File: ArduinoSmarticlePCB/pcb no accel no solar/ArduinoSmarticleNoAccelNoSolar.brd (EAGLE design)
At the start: 48.9 x 17.4 mm, 9 parts

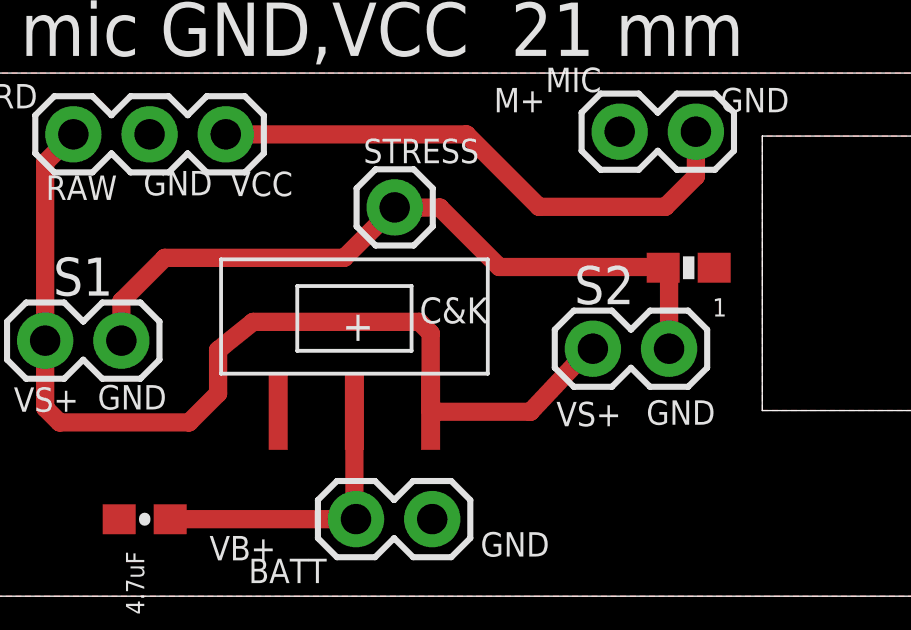
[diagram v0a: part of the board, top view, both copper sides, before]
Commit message: increased isolation size
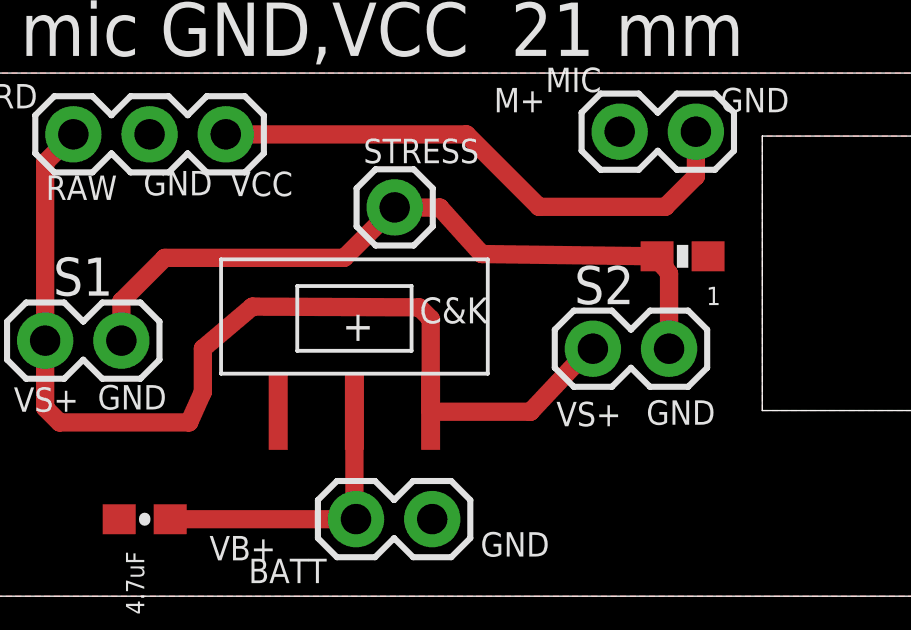
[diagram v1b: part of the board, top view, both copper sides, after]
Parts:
- moved R1 0.43 mm to (35.1, 11.3)
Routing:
- net V_BATT: track 33.8 -> 34.8 mm
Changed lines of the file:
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@@
 <attribute name="NAME" x="16.104821875" y="11.2867625" size="1.27" layer="21" ratio="10" rot="R180"/>
 </element>
-<element name="R1" library="SparkFun-Resistors" package="0603-RES" value="1" x="35.2950625" y="10.9474" smashed="yes" rot="R180">
-<attribute name="PROD_ID" value="RES-08296" x="35.2950625" y="10.9474" size="1.778" layer="27" rot="R180" display="off"/>
-<attribute name="VALUE" value="2.0k" x="35.2950625" y="10.9474" size="1.778" layer="27" rot="R180" display="off"/>
-<attribute name="VALUE" x="36.5650625" y="9.9314" size="0.6096" layer="21" font="vector" rot="R180"/>
+<element name="R1" library="SparkFun-Resistors" package="0603-RES" value="1" x="35.0918625" y="11.3284" smashed="yes" rot="R180">
+<attribute name="PROD_ID" value="RES-08296" x="35.0918625" y="11.3284" size="1.778" layer="27" rot="R180" display="off"/>
+<attribute name="VALUE" value="2.0k" x="35.0918625" y="11.3284" size="1.778" layer="27" rot="R180" display="off"/>
+<attribute name="VALUE" x="36.3618625" y="10.3124" size="0.6096" layer="21" font="vector" rot="R180"/>
 </element>
 <element name="MIC" library="SparkFun-Connectors" package="1X02" value="" x="35.5352" y="15.48288125" smashed="yes" rot="R180">
@@
 <contactref element="BRD" pad="2"/>
 <contactref element="BATT" pad="2"/>
-<polygon width="0.002540625" layer="1" spacing="0.254" isolate="0.3048" thermals="no">
+<polygon width="0.002540625" layer="1" spacing="0.254" isolate="0.6096" thermals="no">
 <vertex x="0.000003125" y="0"/>
 <vertex x="0.000003125" y="6.184659375"/>
@@
 <wire x1="13.844221875" y1="6.272578125" x2="14.3256" y2="5.7912" width="0.6096" layer="1"/>
 <wire x1="14.3256" y1="5.7912" x2="18.6436" y2="5.7912" width="0.6096" layer="1"/>
-<wire x1="18.6436" y1="5.7912" x2="19.6088" y2="6.7564" width="0.6096" layer="1"/>
-<wire x1="19.6088" y1="6.7564" x2="19.6088" y2="8.2042" width="0.6096" layer="1"/>
-<wire x1="19.6088" y1="8.2042" x2="20.7772" y2="9.144" width="0.6096" layer="1"/>
-<wire x1="20.7772" y1="9.144" x2="26.3144" y2="9.144" width="0.6096" layer="1"/>
-<wire x1="26.3144" y1="9.144" x2="26.6954" y2="8.763" width="0.6096" layer="1"/>
-<wire x1="26.6954" y1="8.763" x2="26.6954" y2="6.1493375" width="0.6096" layer="1"/>
+<wire x1="18.6436" y1="5.7912" x2="19.1008" y2="6.8072" width="0.6096" layer="1"/>
+<wire x1="19.1008" y1="6.8072" x2="19.1008" y2="8.255" width="0.6096" layer="1"/>
+<wire x1="19.1008" y1="8.255" x2="20.7518" y2="9.652" width="0.6096" layer="1"/>
+<wire x1="20.7518" y1="9.652" x2="26.3144" y2="9.6266" width="0.6096" layer="1"/>
+<wire x1="26.3144" y1="9.6266" x2="26.6954" y2="9.2456" width="0.6096" layer="1"/>
+<wire x1="26.6954" y1="9.2456" x2="26.6954" y2="6.1493375" width="0.6096" layer="1"/>
 <wire x1="26.6954" y1="6.1493375" x2="26.6928625" y2="6.1468" width="0.6096" layer="1"/>
 <wire x1="26.6928625" y1="6.1468" x2="30.0228" y2="6.1468" width="0.6096" layer="1"/>
@@
 <wire x1="17.8308" y1="11.2776" x2="16.384221875" y2="9.831021875" width="0.6096" layer="1"/>
 <wire x1="16.384221875" y1="9.831021875" x2="16.384221875" y2="8.5181625" width="0.6096" layer="1"/>
-<wire x1="34.6413625" y1="10.7511" x2="34.4450625" y2="10.9474" width="0.6096" layer="1"/>
-<wire x1="34.4450625" y1="10.9474" x2="34.4450625" y2="10.9955375" width="0.6096" layer="1"/>
+<wire x1="34.6413625" y1="10.7511" x2="34.2418625" y2="11.3284" width="0.6096" layer="1"/>
+<wire x1="34.2418625" y1="11.3284" x2="34.4450625" y2="10.9955375" width="0.6096" layer="1"/>
 <wire x1="25.5002625" y1="12.954" x2="25.4948625" y2="12.9594" width="0.6096" layer="1"/>
 <wire x1="34.6413625" y1="10.7511" x2="34.6413625" y2="8.2491375" width="0.6096" layer="1"/>
 <wire x1="25.5002625" y1="12.954" x2="27.0002" y2="12.954" width="0.6096" layer="1"/>
-<wire x1="27.0002" y1="12.954" x2="28.9814" y2="10.9728" width="0.6096" layer="1"/>
-<wire x1="28.9814" y1="10.9728" x2="34.4196625" y2="10.9728" width="0.6096" layer="1"/>
-<wire x1="34.4196625" y1="10.9728" x2="34.4450625" y2="10.9474" width="0.6096" layer="1"/>
+<wire x1="27.0002" y1="12.954" x2="28.3972" y2="11.4046" width="0.6096" layer="1"/>
+<wire x1="28.3972" y1="11.4046" x2="34.2418625" y2="11.3284" width="0.6096" layer="1"/>
 </signal>
 <signal name="SWITCH+">

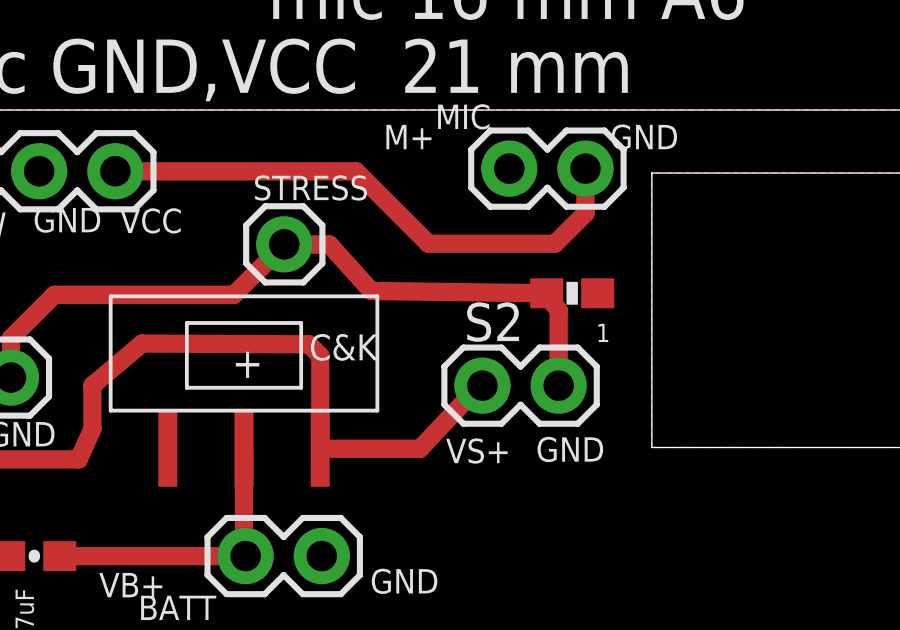
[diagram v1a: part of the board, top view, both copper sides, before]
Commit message: symmetrized path still need to remove concave corners
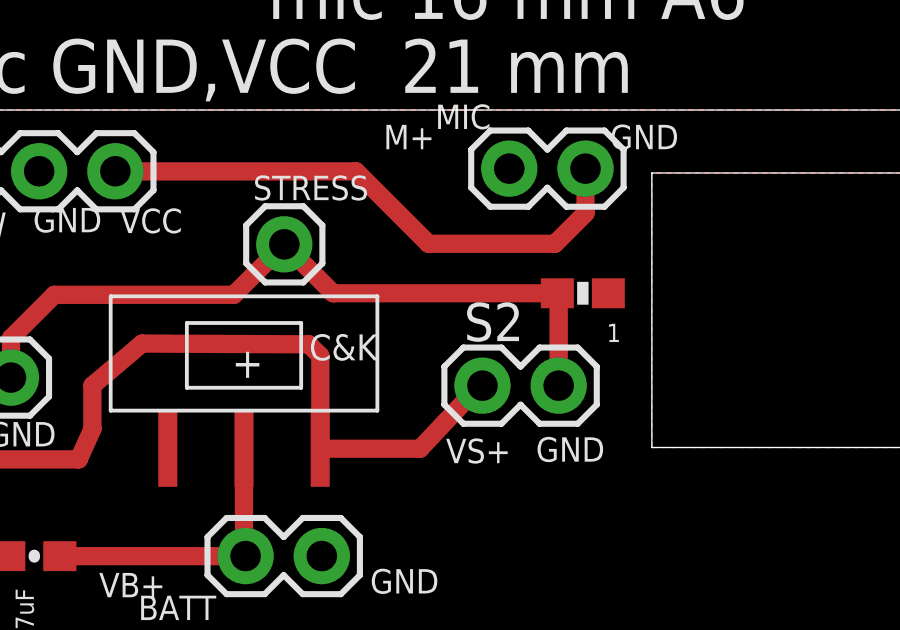
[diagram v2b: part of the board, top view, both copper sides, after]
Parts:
- moved R1 0.36 mm to (35.4, 11.3)
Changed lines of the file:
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@@
 <attribute name="NAME" x="16.104821875" y="11.2867625" size="1.27" layer="21" ratio="10" rot="R180"/>
 </element>
-<element name="R1" library="SparkFun-Resistors" package="0603-RES" value="1" x="35.0918625" y="11.3284" smashed="yes" rot="R180">
-<attribute name="PROD_ID" value="RES-08296" x="35.0918625" y="11.3284" size="1.778" layer="27" rot="R180" display="off"/>
-<attribute name="VALUE" value="2.0k" x="35.0918625" y="11.3284" size="1.778" layer="27" rot="R180" display="off"/>
-<attribute name="VALUE" x="36.3618625" y="10.3124" size="0.6096" layer="21" font="vector" rot="R180"/>
+<element name="R1" library="SparkFun-Resistors" package="0603-RES" value="1" x="35.4474625" y="11.3284" smashed="yes" rot="R180">
+<attribute name="PROD_ID" value="RES-08296" x="35.4474625" y="11.3284" size="1.778" layer="27" rot="R180" display="off"/>
+<attribute name="VALUE" value="2.0k" x="35.4474625" y="11.3284" size="1.778" layer="27" rot="R180" display="off"/>
+<attribute name="VALUE" x="36.7174625" y="10.3124" size="0.6096" layer="21" font="vector" rot="R180"/>
 </element>
 <element name="MIC" library="SparkFun-Connectors" package="1X02" value="" x="35.5352" y="15.48288125" smashed="yes" rot="R180">
@@
 <contactref element="S2" pad="1"/>
 <contactref element="S1" pad="1"/>
-<wire x1="34.6684625" y1="8.2762375" x2="34.6413625" y2="8.2491375" width="0.4064" layer="1"/>
 <wire x1="25.4948625" y1="12.9594" x2="23.8130625" y2="11.2776" width="0.6096" layer="1"/>
 <wire x1="23.8130625" y1="11.2776" x2="17.8308" y2="11.2776" width="0.6096" layer="1"/>
 <wire x1="17.8308" y1="11.2776" x2="16.384221875" y2="9.831021875" width="0.6096" layer="1"/>
 <wire x1="16.384221875" y1="9.831021875" x2="16.384221875" y2="8.5181625" width="0.6096" layer="1"/>
-<wire x1="34.6413625" y1="10.7511" x2="34.2418625" y2="11.3284" width="0.6096" layer="1"/>
-<wire x1="34.2418625" y1="11.3284" x2="34.4450625" y2="10.9955375" width="0.6096" layer="1"/>
-<wire x1="25.5002625" y1="12.954" x2="25.4948625" y2="12.9594" width="0.6096" layer="1"/>
-<wire x1="34.6413625" y1="10.7511" x2="34.6413625" y2="8.2491375" width="0.6096" layer="1"/>
-<wire x1="25.5002625" y1="12.954" x2="27.0002" y2="12.954" width="0.6096" layer="1"/>
-<wire x1="27.0002" y1="12.954" x2="28.3972" y2="11.4046" width="0.6096" layer="1"/>
-<wire x1="28.3972" y1="11.4046" x2="34.2418625" y2="11.3284" width="0.6096" layer="1"/>
+<wire x1="34.5974625" y1="11.3284" x2="27.1258625" y2="11.3284" width="0.6096" layer="1"/>
+<wire x1="27.1258625" y1="11.3284" x2="25.4948625" y2="12.9594" width="0.6096" layer="1"/>
+<wire x1="34.6413625" y1="8.2491375" x2="34.6413625" y2="11.2845" width="0.6096" layer="1"/>
+<wire x1="34.6413625" y1="11.2845" x2="34.5974625" y2="11.3284" width="0.6096" layer="1"/>
 </signal>
 <signal name="SWITCH+">

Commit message: Merediths changes to the PCB, now can be milled on the othermill successfully downstairs
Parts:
- moved S2 4.32 mm to (34.6, 3.93)
- moved R1 2.11 mm to (35.5, 9.22)
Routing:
- net SERVOGND: track 24.6 -> 29.5 mm
- net V_BATT: track 34.8 -> 36.3 mm
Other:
- board text added: "Battery 45mm"
- board text added: "Mic 16mm A6"
- board text added: "Mic GND,VCC 26mm, 26 mm"
- board text added: "RAW, GND, VCC 26mm"
- board text added: "S1 SIG, 48 mm D5"
- board text added: "S1 VCC,GND, 37,38mm"
- board text added: "S2 SIG, 52mm D6"
- board text added: "S2 VCC,GND, 37,38mm"
- board text added: "Stress 28 A7"
- board text removed: "RAW,GND,VCC 26 mm"
- board text removed: "S1 SIG,48 mm D5"
- board text removed: "S1 SIG,52 mm D6"
- board text removed: "S1 VCC,GND 37,38 mm"
- board text removed: "S2 VCC,GND 37,38 mm"
- board text removed: "battery 45 mm"
- board text removed: "mic 16 mm A6"
- board text removed: "mic GND,VCC 21 mm"
- board text removed: "stress 28 mm A7"
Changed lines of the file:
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@@
 <setting verticaltext="up"/>
 </settings>
-<grid distance="0.001" unitdist="inch" unit="inch" style="lines" multiple="1" display="yes" altdistance="0.0001" altunitdist="inch" altunit="inch"/>
+<grid distance="50" unitdist="mil" unit="mil" style="lines" multiple="1" display="no" altdistance="5" altunitdist="mil" altunit="mil"/>
 <layers>
 <layer number="1" name="Top" color="4" fill="1" visible="yes" active="yes"/>
@@
 <text x="23.7464625" y="8.509" size="1.016" layer="21">+</text>
 <text x="21.5366625" y="2.0066" size="0.8128" layer="21" rot="R180">VB+</text>
-<text x="30.6552625" y="2.1336" size="0.8128" layer="21" rot="R180">GND</text>
-<text x="33.8810625" y="5.715" size="0.8128" layer="21">GND</text>
-<text x="30.8838625" y="5.6642" size="0.8128" layer="21">VS+</text>
+<text x="29.3852625" y="0.8636" size="0.8128" layer="21" rot="R180">GND</text>
+<text x="34.2620625" y="1.524" size="0.8128" layer="21">GND</text>
+<text x="31.0108625" y="1.3462" size="0.8128" layer="21">VS+</text>
 <text x="13.8658625" y="13.208" size="0.8128" layer="21">RAW</text>
 <text x="17.1170625" y="13.3604" size="0.8128" layer="21">GND</text>
@@
 <text x="28.8010625" y="16.129" size="0.8128" layer="21">M+</text>
 <wire x1="11.7474625" y1="6.1872" x2="-0.0025375" y2="6.188121875" width="0" layer="20"/>
-<text x="36.9544625" y="29.21" size="1.778" layer="21" rot="R180">RAW,GND,VCC 26 mm</text>
-<text x="37.0052625" y="26.6446" size="1.778" layer="21" rot="R180">battery 45 mm</text>
-<text x="40.8406625" y="24.4094" size="1.778" layer="21" rot="R180">stress 28 mm A7</text>
-<text x="40.9422625" y="22.2504" size="1.778" layer="21" rot="R180">mic 16 mm A6</text>
-<text x="37.5894625" y="-1.4478" size="1.778" layer="21" rot="R180">S1 VCC,GND 37,38 mm</text>
-<text x="41.5518625" y="-6.3754" size="1.778" layer="21" rot="R180">S1 SIG,48 mm D5</text>
-<text x="41.5264625" y="-8.7884" size="1.778" layer="21" rot="R180">S1 SIG,52 mm D6</text>
-<text x="37.6402625" y="-3.9624" size="1.778" layer="21" rot="R180">S2 VCC,GND 37,38 mm</text>
-<text x="37.1322625" y="19.7866" size="1.778" layer="21" rot="R180">mic GND,VCC  21 mm</text>
+<text x="17.78" y="30.48" size="1.778" layer="21">RAW, GND, VCC 26mm</text>
+<text x="17.78" y="27.94" size="1.778" layer="21">Battery 45mm</text>
+<text x="17.78" y="25.4" size="1.778" layer="21">Stress 28 A7</text>
+<text x="17.78" y="22.86" size="1.778" layer="21">Mic 16mm A6</text>
+<text x="17.78" y="-2.54" size="1.778" layer="21">S1 VCC,GND, 37,38mm</text>
+<text x="17.78" y="20.32" size="1.778" layer="21">Mic GND,VCC 26mm, 26 mm</text>
+<text x="17.78" y="-5.08" size="1.778" layer="21">S2 VCC,GND, 37,38mm</text>
+<text x="17.78" y="-7.62" size="1.778" layer="21">S1 SIG, 48 mm D5</text>
+<text x="17.78" y="-10.16" size="1.778" layer="21">S2 SIG, 52mm D6</text>
 </plain>
 <attributes>
@@
 <attribute name="VALUE" x="16.538" y="1.4935375" size="0.6096" layer="21" font="vector" rot="R270"/>
 </element>
-<element name="S2" library="SparkFun-Connectors" package="1X02" value="" x="34.6413625" y="8.2491375" smashed="yes" rot="R180">
-<attribute name="NAME" x="33.4763625" y="11.0040625" size="1.27" layer="21" ratio="10" rot="R180"/>
-<attribute name="VALUE" x="35.9113625" y="11.4241375" size="1.27" layer="27" rot="R180"/>
+<element name="S2" library="SparkFun-Connectors" package="1X02" value="" x="34.6413625" y="3.9311375" smashed="yes" rot="R180">
+<attribute name="NAME" x="33.4763625" y="6.6860625" size="1.27" layer="21" ratio="10" rot="R180"/>
+<attribute name="VALUE" x="35.9113625" y="7.1061375" size="1.27" layer="27" rot="R180"/>
 </element>
 <element name="S1" library="SparkFun-Connectors" package="1X02" value="S1" x="16.384221875" y="8.5181625" smashed="yes" rot="R180">
 <attribute name="NAME" x="16.104821875" y="11.2867625" size="1.27" layer="21" ratio="10" rot="R180"/>
 </element>
-<element name="R1" library="SparkFun-Resistors" package="0603-RES" value="1" x="35.4474625" y="11.3284" smashed="yes" rot="R180">
-<attribute name="PROD_ID" value="RES-08296" x="35.4474625" y="11.3284" size="1.778" layer="27" rot="R180" display="off"/>
-<attribute name="VALUE" value="2.0k" x="35.4474625" y="11.3284" size="1.778" layer="27" rot="R180" display="off"/>
-<attribute name="VALUE" x="36.7174625" y="10.3124" size="0.6096" layer="21" font="vector" rot="R180"/>
+<element name="R1" library="SparkFun-Resistors" package="0603-RES" value="1" x="35.5236625" y="9.2202" smashed="yes" rot="R180">
+<attribute name="PROD_ID" value="RES-08296" x="35.5236625" y="9.2202" size="1.778" layer="27" rot="R180" display="off"/>
+<attribute name="VALUE" value="2.0k" x="35.5236625" y="9.2202" size="1.778" layer="27" rot="R180" display="off"/>
+<attribute name="VALUE" x="36.7936625" y="8.2042" size="0.6096" layer="21" font="vector" rot="R180"/>
 </element>
 <element name="MIC" library="SparkFun-Connectors" package="1X02" value="" x="35.5352" y="15.48288125" smashed="yes" rot="R180">
@@
 </element>
 <element name="BATT" library="SparkFun-Connectors" package="1X02" value="" x="24.206015625" y="2.568659375" smashed="yes">
-<attribute name="NAME" x="20.624615625" y="0.435059375" size="0.8128" layer="21" ratio="10"/>
+<attribute name="NAME" x="21.894615625" y="0.435059375" size="0.8128" layer="21" ratio="10"/>
 <attribute name="VALUE" x="22.936015625" y="-0.606340625" size="1.27" layer="27"/>
 </element>
@@
 <wire x1="20.7518" y1="9.652" x2="26.3144" y2="9.6266" width="0.6096" layer="1"/>
 <wire x1="26.3144" y1="9.6266" x2="26.6954" y2="9.2456" width="0.6096" layer="1"/>
-<wire x1="26.6954" y1="9.2456" x2="26.6954" y2="6.1493375" width="0.6096" layer="1"/>
-<wire x1="26.6954" y1="6.1493375" x2="26.6928625" y2="6.1468" width="0.6096" layer="1"/>
-<wire x1="26.6928625" y1="6.1468" x2="30.0228" y2="6.1468" width="0.6096" layer="1"/>
-<wire x1="30.0228" y1="6.1468" x2="31.9981375" y2="8.2491375" width="0.6096" layer="1"/>
-<wire x1="31.9981375" y1="8.2491375" x2="32.1013625" y2="8.2491375" width="0.6096" layer="1"/>
+<wire x1="26.6954" y1="7.4193375" x2="26.6954" y2="9.2456" width="0.6096" layer="1"/>
+<wire x1="26.6954" y1="7.4193375" x2="26.6928625" y2="6.1468" width="0.6096" layer="1"/>
 <wire x1="13.844221875" y1="8.5181625" x2="13.844221875" y2="14.455159375" width="0.6096" layer="1"/>
 <wire x1="13.844221875" y1="14.455159375" x2="14.7846625" y2="15.3956" width="0.6096" layer="1"/>
+<wire x1="32.1013625" y1="3.9311375" x2="32.1013625" y2="5.9986375" width="0.6096" layer="1"/>
+<wire x1="32.1013625" y1="5.9986375" x2="31.75" y2="6.35" width="0.6096" layer="1"/>
+<wire x1="31.75" y1="6.35" x2="26.8960625" y2="7.62" width="0.6096" layer="1"/>
+<wire x1="26.8960625" y1="7.62" x2="26.6954" y2="7.4193375" width="0.6096" layer="1"/>
 </signal>
 <signal name="VCC">
@@
 <wire x1="35.5352" y1="15.48288125" x2="35.5352" y2="13.996" width="0.6096" layer="1"/>
 <wire x1="35.5352" y1="13.996" x2="34.5186" y2="12.9794" width="0.6096" layer="1"/>
-<wire x1="34.5186" y1="12.9794" x2="30.3022" y2="12.9794" width="0.6096" layer="1"/>
-<wire x1="30.3022" y1="12.9794" x2="27.8892" y2="15.3924" width="0.6096" layer="1"/>
-<wire x1="27.8892" y1="15.3924" x2="19.8678625" y2="15.3924" width="0.6096" layer="1"/>
+<wire x1="34.5186" y1="12.9794" x2="31.5722" y2="12.9794" width="0.6096" layer="1"/>
+<wire x1="31.5722" y1="12.9794" x2="29.1592" y2="15.3924" width="0.6096" layer="1"/>
+<wire x1="29.1592" y1="15.3924" x2="19.8678625" y2="15.3924" width="0.6096" layer="1"/>
 <wire x1="19.8678625" y1="15.3924" x2="19.8646625" y2="15.3956" width="0.6096" layer="1"/>
 </signal>
@@
 <contactref element="S2" pad="1"/>
 <contactref element="S1" pad="1"/>
-<wire x1="25.4948625" y1="12.9594" x2="23.8130625" y2="11.2776" width="0.6096" layer="1"/>
-<wire x1="23.8130625" y1="11.2776" x2="17.8308" y2="11.2776" width="0.6096" layer="1"/>
-<wire x1="17.8308" y1="11.2776" x2="16.384221875" y2="9.831021875" width="0.6096" layer="1"/>
-<wire x1="16.384221875" y1="9.831021875" x2="16.384221875" y2="8.5181625" width="0.6096" layer="1"/>
-<wire x1="34.5974625" y1="11.3284" x2="27.1258625" y2="11.3284" width="0.6096" layer="1"/>
-<wire x1="27.1258625" y1="11.3284" x2="25.4948625" y2="12.9594" width="0.6096" layer="1"/>
-<wire x1="34.6413625" y1="8.2491375" x2="34.6413625" y2="11.2845" width="0.6096" layer="1"/>
-<wire x1="34.6413625" y1="11.2845" x2="34.5974625" y2="11.3284" width="0.6096" layer="1"/>
+<wire x1="25.57713125" y1="12.87713125" x2="25.4948625" y2="12.9594" width="0.6096" layer="1"/>
+<wire x1="34.6413625" y1="3.9311375" x2="34.6413625" y2="9.1879" width="0.6096" layer="1"/>
+<wire x1="34.6413625" y1="9.1879" x2="34.6736625" y2="9.2202" width="0.6096" layer="1"/>
+<wire x1="16.384221875" y1="8.5181625" x2="16.384221875" y2="12.574221875" width="0.6096" layer="1"/>
+<wire x1="16.384221875" y1="12.574221875" x2="16.51" y2="12.7" width="0.6096" layer="1"/>
+<wire x1="25.4" y1="12.7" x2="16.51" y2="12.7" width="0.6096" layer="1"/>
+<wire x1="25.4" y1="12.7" x2="25.57713125" y2="12.87713125" width="0.6096" layer="1"/>
+<wire x1="34.6736625" y1="9.2202" x2="31.4198" y2="9.2202" width="0.6096" layer="1"/>
+<wire x1="31.4198" y1="9.2202" x2="27.94" y2="12.7" width="0.6096" layer="1"/>
+<wire x1="27.94" y1="12.7" x2="25.4" y2="12.7" width="0.6096" layer="1"/>
 </signal>
 <signal name="SWITCH+">
